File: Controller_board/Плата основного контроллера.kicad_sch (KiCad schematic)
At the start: 41 parts, among them Q1 DTC114ECA, Q2 DTC114ECA, U1 ADM3485EARZ-REEL, U2 ISO6741FDWR, U4 AM1SS-2403SJZ, U5 AM1SS-2405SJZ

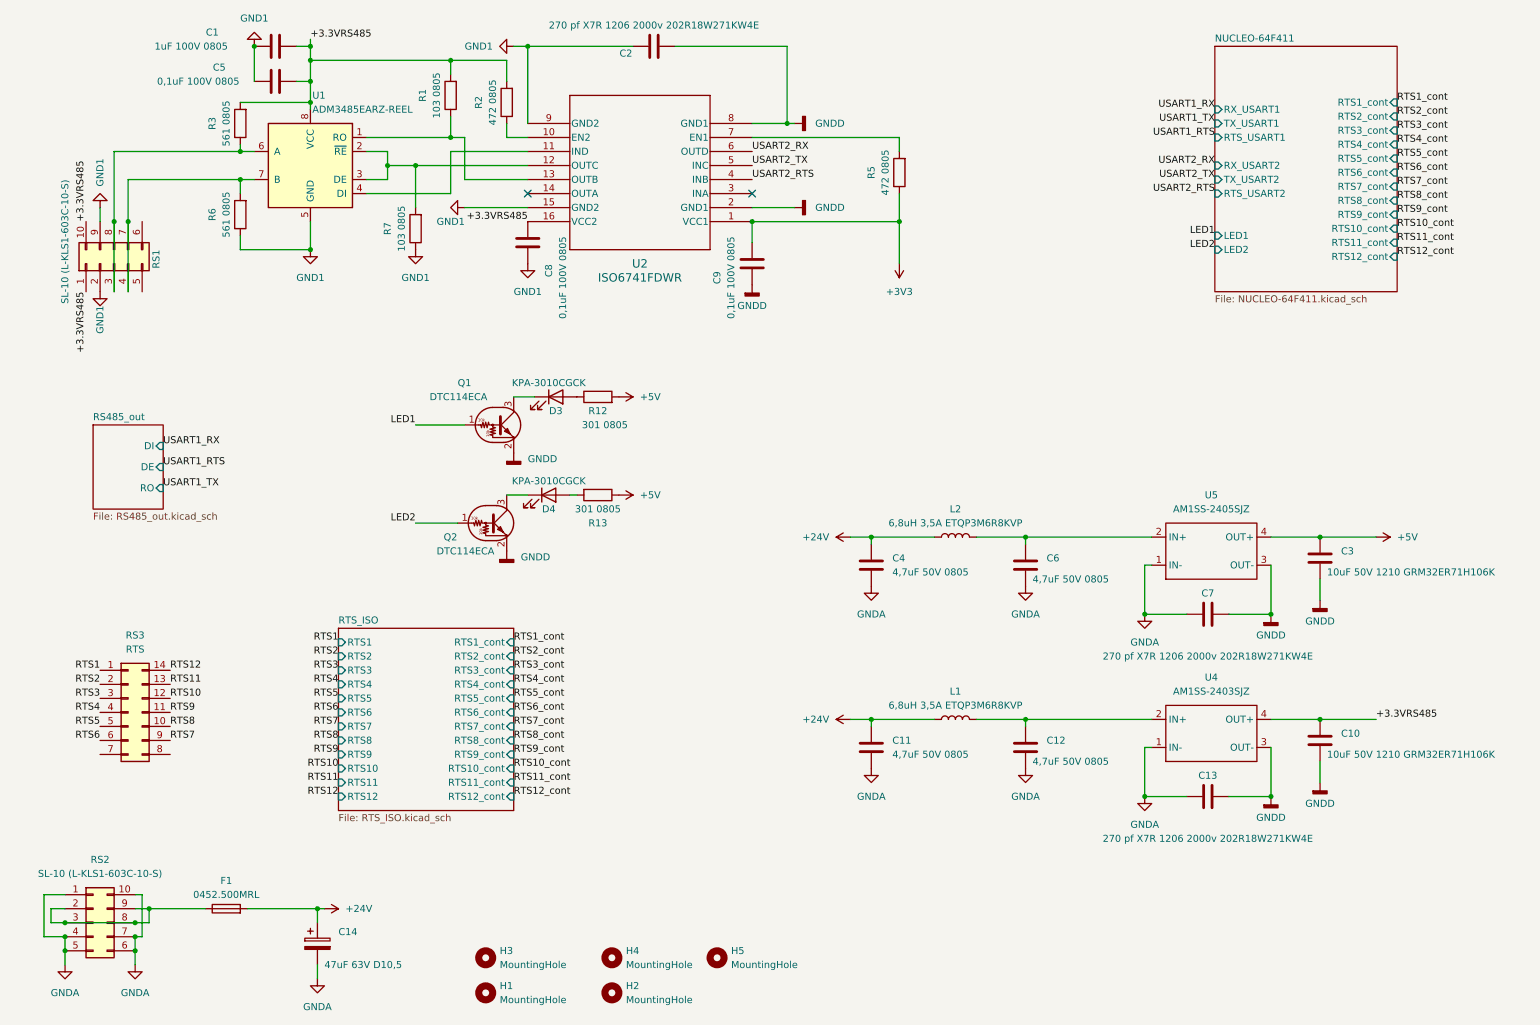
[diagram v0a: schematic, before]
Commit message: Modify Digit_IN, Motherbord, Step motors, photo
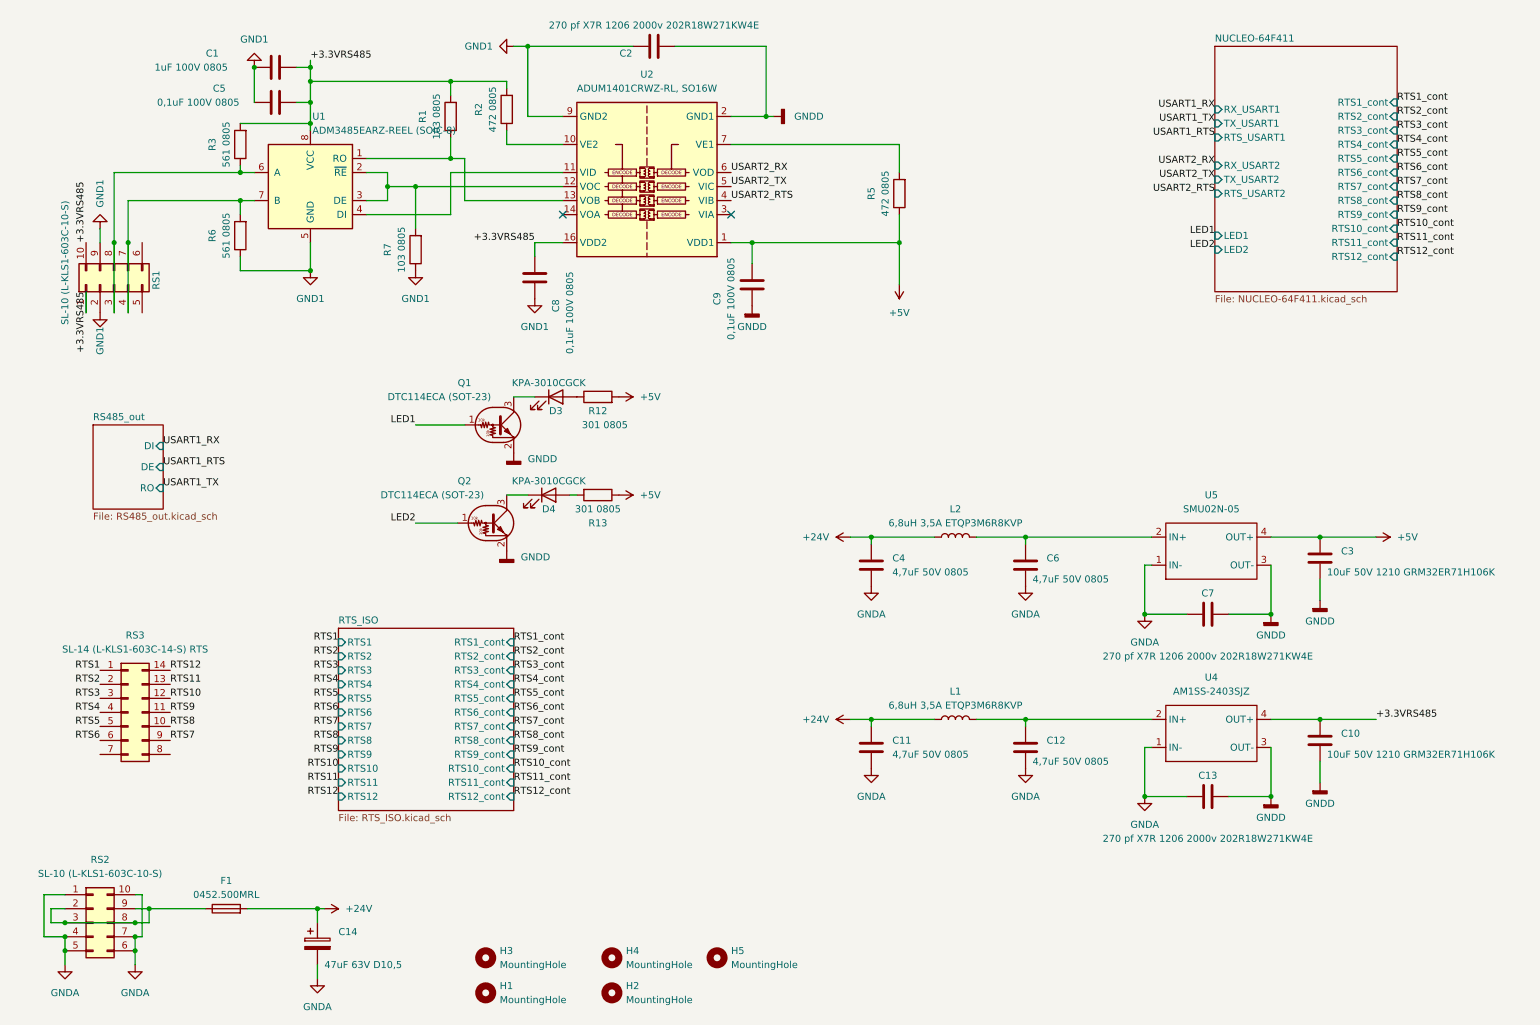
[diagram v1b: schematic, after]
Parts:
- removed U2: ISO6741FDWR, PCM_Package_SO_AKL:SOIC-16W_7.5x10.3mm_P1.27mm, symbol Isolator:ISO6741FDWR
- added U2: ADUM1401CRWZ-RL, SO16W, Package_SO:SOIC-16W_7.5x10.3mm_P1.27mm, symbol Isolator:ADuM1401xRW
- Q1, Q2: value DTC114ECA -> DTC114ECA (SOT-23)
- RS3: value RTS -> SL-14 (L-KLS1-603C-14-S) RTS
- U1: value ADM3485EARZ-REEL -> ADM3485EARZ-REEL (SOIC-8)
- U4: footprint Converter_DCDC:Converter_DCDC_Murata_MEE3SxxxxSC_THT -> Converter_DCDC:Converter_DCDC_Murata_CRE1xxxxxxSC_THT
- U5: value AM1SS-2405SJZ -> SMU02N-05; footprint Converter_DCDC:Converter_DCDC_Murata_MEE3SxxxxSC_THT -> Converter_DCDC:Converter_DCDC_Murata_CRE1xxxxxxSC_THT
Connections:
- net +3V3 is gone; now on net +5V: C9.2, R5.1
- net +3.3VRS485: now also U2.16 (VDD2)
- net +5V: now also U2.1 (VDD1)
- net GND1: now also U2.15 (GND2), U2.9 (GND2)
- net GNDD: now also U2.2 (GND1), U2.8 (GND1)
- net USART2_RTS: now also U2.4 (VIB)
- net USART2_RX: now also U2.6 (VOD)
- net USART2_TX: now also U2.5 (VIC)
- net at R2.1: now also U2.10 (VE2)
- net at U1.4 (DI): now also U2.11 (VID)
- net at R7.2, U1.2 (~{RE}), U1.3 (DE): now also U2.12 (VOC)
- net at R1.1, U1.1 (RO): now also U2.13 (VOB)
- net at R5.2: now also U2.7 (VE1)
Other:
- moved on the sheet: C1, C5, C8, C9, R1, R2, R3, R5, R6, R7, RS1, U1

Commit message: Modify MainController Schems and PCB1
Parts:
- removed C10: 10uF 50V 1210 GRM32ER71H106K, PCM_Capacitor_SMD_AKL:C_1210_3225Metric_Pad1.42x2.65mm_HandSolder, symbol Device:C
- removed C11, C12: 4,7uF 50V 0805, PCM_Capacitor_SMD_AKL:C_0805_2012Metric_Pad1.18x1.45mm_HandSolder, symbol Device:C
- removed C13: 270 pf X7R 1206 2000v 202R18W271KW4E, PCM_Capacitor_SMD_Handsoldering_AKL:C_1210_3225Metric_Pad1.42x2.65mm, symbol Device:C
- removed L1: 6,8uH 3,5A ETQP3M6R8KVP, PCM_Inductor_SMD_Handsoldering_AKL:L_Bourns-SRN6028, symbol Device:L
- removed U4: AM1SS-2403SJZ, Converter_DCDC:Converter_DCDC_Murata_CRE1xxxxxxSC_THT, symbol Converter_DCDC:AM1SS-
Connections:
- net USART2_RTS: now also U2.5 (VIC); no longer U2.4 (VIB)
- net USART2_TX: now also U2.4 (VIB); no longer U2.5 (VIC)
- net at R1.1, U1.1 (RO): now also U2.11 (VID); no longer U2.13 (VOB)
- net at U1.4 (DI): now also U2.13 (VOB); no longer U2.11 (VID)

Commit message: Modify Mian controller, stepmotor, motor 25.05.24
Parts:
- added J3: DebugUSART (PinHeader_01x02_P2.54mm), Connector_PinHeader_2.54mm:PinHeader_1x02_P2.54mm_Vertical, symbol Connector:Conn_01x02_Pin
- added J4: Debug GPIO (PinHeader_01x02_P2.54mm), Connector_PinHeader_2.54mm:PinHeader_1x02_P2.54mm_Vertical, symbol Connector:Conn_01x02_Pin
- added R31: 121 0805, PCM_4ms_Resistor:R_0805_2012Metric, symbol Device:R
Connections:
- net RTS10: now also RS3.10 (Pin_10); no longer RS3.12 (Pin_12)
- net RTS11: now also RS3.6 (Pin_6); no longer RS3.13 (Pin_13)
- net RTS12: now also RS3.9 (Pin_9); no longer RS3.14 (Pin_14)
- net RTS2: now also RS3.14 (Pin_14); no longer RS3.2 (Pin_2)
- net RTS3: now also RS3.2 (Pin_2); no longer RS3.3 (Pin_3)
- net RTS4: now also RS3.13 (Pin_13); no longer RS3.4 (Pin_4)
- net RTS5: now also RS3.3 (Pin_3); no longer RS3.5 (Pin_5)
- net RTS6: now also RS3.12 (Pin_12); no longer RS3.6 (Pin_6)
- net RTS7: now also RS3.4 (Pin_4); no longer RS3.9 (Pin_9)
- net RTS8: now also RS3.11 (Pin_11); no longer RS3.10 (Pin_10)
- net RTS9: now also RS3.5 (Pin_5); no longer RS3.11 (Pin_11)
- net at R3.1, RS1.3 (Pin_3), RS1.8 (Pin_8)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: now also R31.2
- net at R6.2, RS1.4 (Pin_4), RS1.7 (Pin_7)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: now also R31.1
- new net GPIO1: J4.1 (Pin_1)
- new net GPIO2: J4.2 (Pin_2)
- new net USART6_RX: J3.2 (Pin_2)
- new net USART6_TX: J3.1 (Pin_1)
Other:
- sheet NUCLEO-64F411 ports: added GPIO1, GPIO2, RTS_USART6, RX_USART6, TX_USART6; removed none
- sheet RS485_out ports: added RX, TX; removed DI, RO
- moved on the sheet: C2, C8, C9, D4, Q2, R1, R13, R2, R5, U2

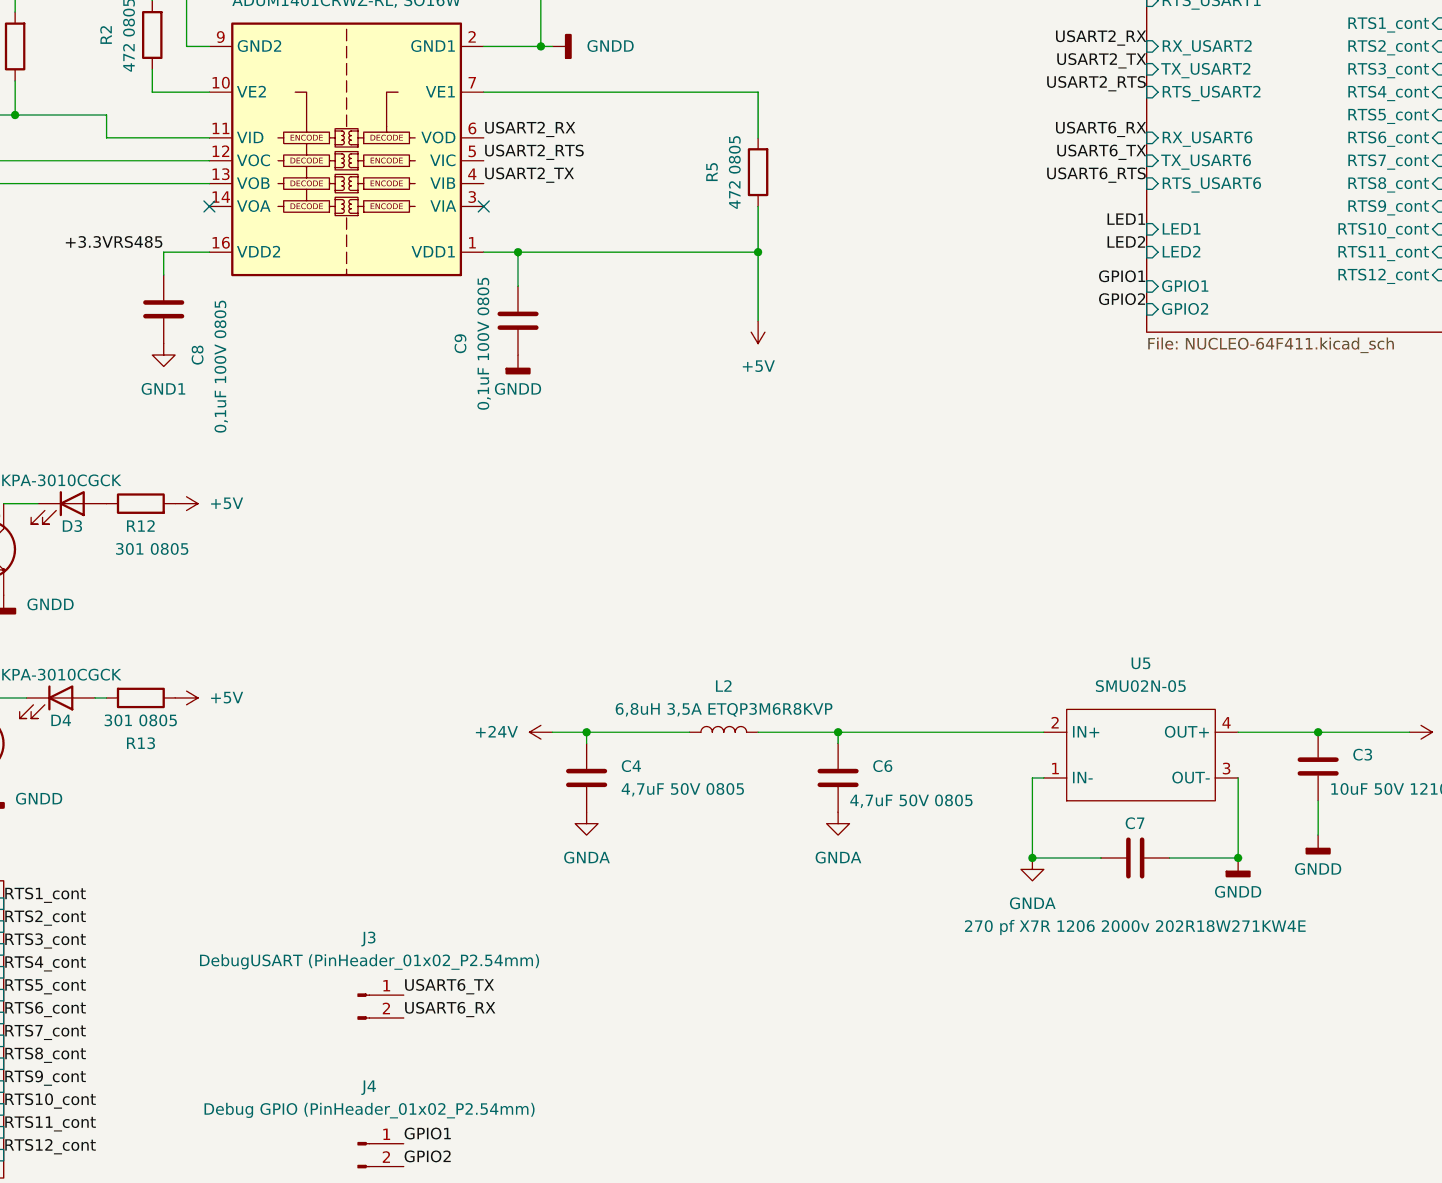
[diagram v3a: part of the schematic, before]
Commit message: Add DE USART 03.06.24
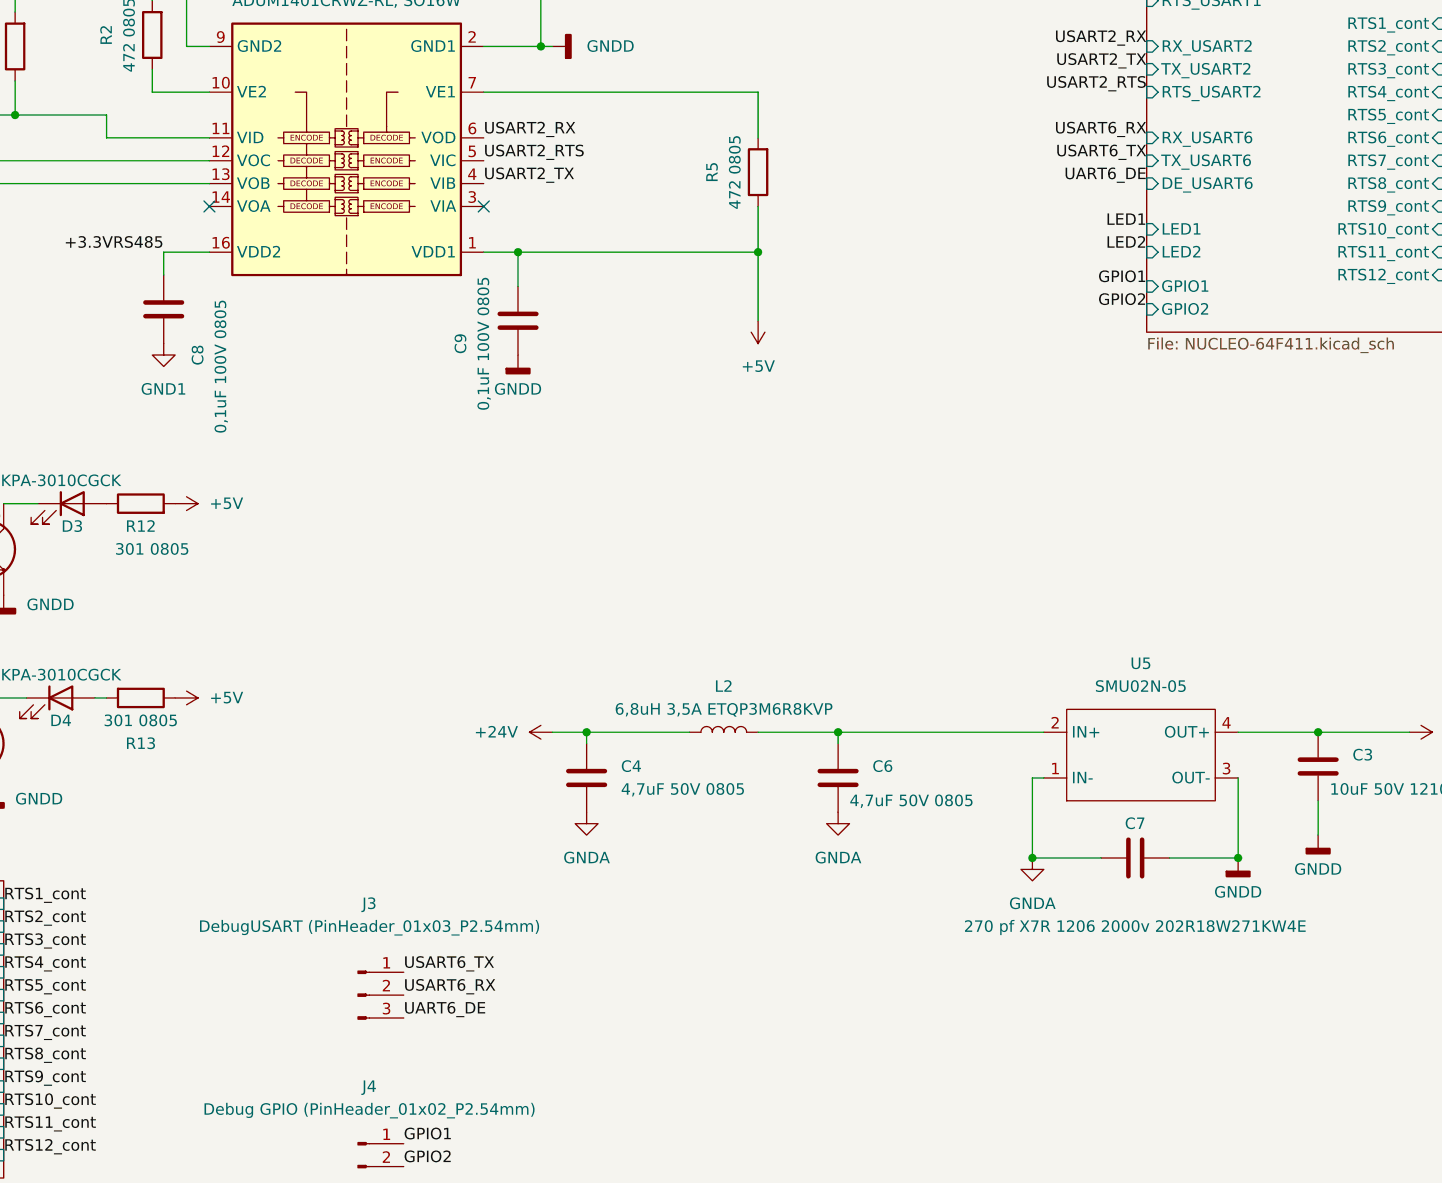
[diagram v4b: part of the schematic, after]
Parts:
- J3: value DebugUSART (PinHeader_01x02_P2.54mm) -> DebugUSART (PinHeader_01x03_P2.54mm); footprint Connector_PinHeader_2.54mm:PinHeader_1x02_P2.54mm_Vertical -> Connector_PinHeader_2.54mm:PinHeader_1x03_P2.54mm_Vertical; symbol Connector:Conn_01x02_Pin -> Connector:Conn_01x03_Pin
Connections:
- new net UART6_DE: J3.3 (Pin_3)
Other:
- sheet NUCLEO-64F411 ports: added DE_USART6; removed RTS_USART6
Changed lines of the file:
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@@
     (effects (font (size 1.27 1.27)) (justify left bottom))
   )
-  (label "USART6_TX" (at 144.78 138.43 0) (fields_autoplaced)
+  (label "USART6_TX" (at 144.78 135.89 0) (fields_autoplaced)
     (effects (font (size 1.27 1.27)) (justify left bottom))
   )
@@
     (effects (font (size 1.27 1.27)) (justify left bottom))
   )
-  (label "USART6_RX" (at 144.78 140.97 0) (fields_autoplaced)
+  (label "USART6_RX" (at 144.78 138.43 0) (fields_autoplaced)
     (effects (font (size 1.27 1.27)) (justify left bottom))
   )
@@
     (effects (font (size 1.27 1.27)) (justify left bottom))
   )
-  (label "USART6_RTS" (at 227.33 48.26 180) (fields_autoplaced)
-    (effects (font (size 1.27 1.27)) (justify right bottom))
-  )
   (label "LED2" (at 82.55 110.49 180) (fields_autoplaced)
     (effects (font (size 1.27 1.27)) (justify right bottom))
@@
     (effects (font (size 1.27 1.27)) (justify right bottom))
   )
+  (label "UART6_DE" (at 144.78 140.97 0) (fields_autoplaced)
+    (effects (font (size 1.27 1.27)) (justify left bottom))
+  )
   (label "USART1_RX" (at 36.83 92.71 0) (fields_autoplaced)
     (effects (font (size 1.27 1.27)) (justify left bottom))
@@
   )
   (label "USART2_RX" (at 227.33 33.02 180) (fields_autoplaced)
+    (effects (font (size 1.27 1.27)) (justify right bottom))
+  )
+  (label "UART6_DE" (at 227.33 48.26 180) (fields_autoplaced)
     (effects (font (size 1.27 1.27)) (justify right bottom))
   )
@@
     )
   )
-  (symbol (lib_id "Connector:Conn_01x02_Pin") (at 139.7 138.43 0) (unit 1)
-    (in_bom yes) (on_board yes) (dnp no)
-    (property "Reference" "J3" (at 140.97 132.08 0)
-      (effects (font (size 1.27 1.27)))
-    )
-    (property "Value" "DebugUSART (PinHeader_01x02_P2.54mm)" (at 140.97 134.62 0)
-      (effects (font (size 1.27 1.27)))
-    )
-    (property "Footprint" "Connector_PinHeader_2.54mm:PinHeader_1x02_P2.54mm_Vertical" (at 139.7 138.43 0)
+  (symbol (lib_id "Connector:Conn_01x03_Pin") (at 139.7 138.43 0) (unit 1)
+    (in_bom yes) (on_board yes) (dnp no)
+    (property "Reference" "J3" (at 140.97 128.27 0)
+      (effects (font (size 1.27 1.27)))
+    )
+    (property "Value" "DebugUSART (PinHeader_01x03_P2.54mm)" (at 140.97 130.81 0)
+      (effects (font (size 1.27 1.27)))
+    )
+    (property "Footprint" "Connector_PinHeader_2.54mm:PinHeader_1x03_P2.54mm_Vertical" (at 139.7 138.43 0)
       (effects (font (size 1.27 1.27)) hide)
     )
@@
     (pin "1")
     (pin "2")
+    (pin "3")
     (instances
       (project "Плата основного контроллера"
@@
       (effects (font (size 1.27 1.27)) (justify left))
     )
-    (pin "RTS_USART6" input (at 227.33 48.26 180)
-      (effects (font (size 1.27 1.27)) (justify left))
-    )
+    (pin "DE_USART6" input (at 227.33 48.26 180)
+      (effects (font (size 1.27 1.27)) (justify left))
+    )
